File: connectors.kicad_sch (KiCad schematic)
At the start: 11 parts, among them J1 DE9_Pins_MountingHoles, J10 Conn_01x08_Socket, J11 Conn_01x08_Socket, J2 Conn_01x08_Socket, J3 HPF-02-01-X-S, J4 Conn_01x04_Socket, J5 Conn_01x04_Socket, J6 Conn_01x04_Socket, J7 Conn_01x04_Socket, J8 Conn_01x02_Pin, J9 Conn_01x02_Pin

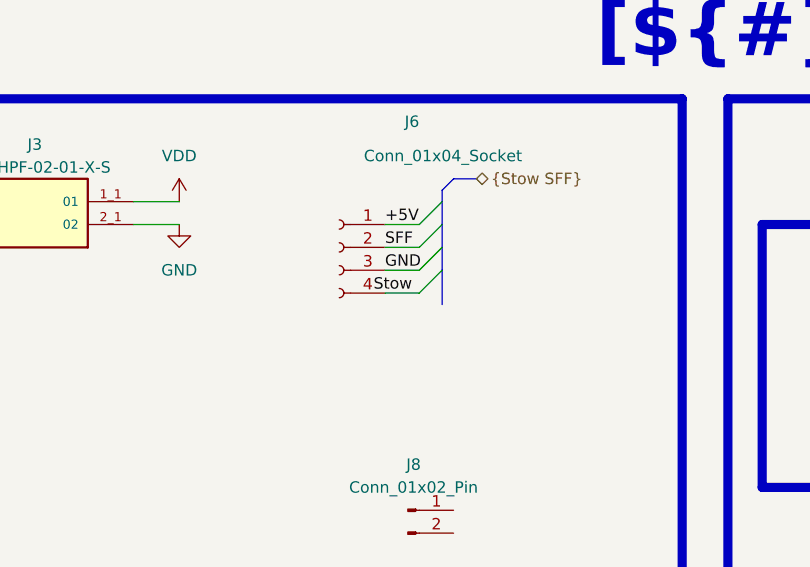
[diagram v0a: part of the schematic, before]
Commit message: updated architecture page
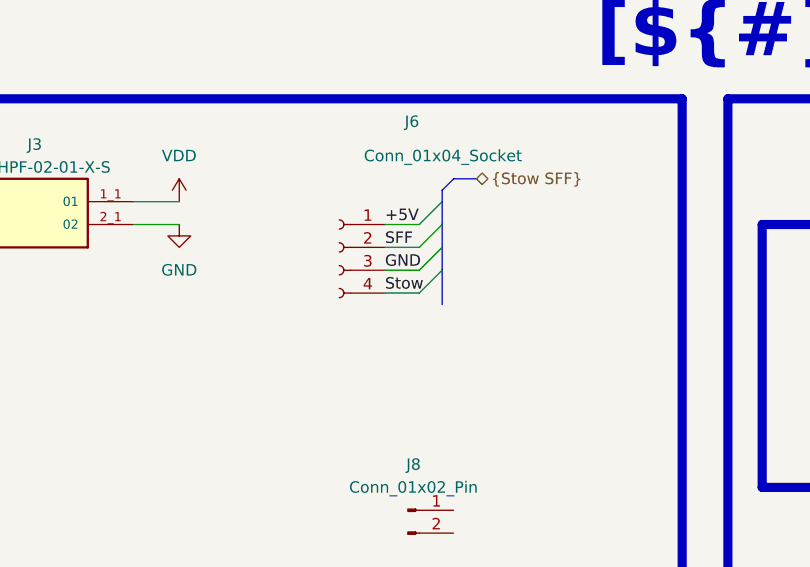
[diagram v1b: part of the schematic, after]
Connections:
- net Stow: now also J6.4 (Pin_4)
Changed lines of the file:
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@@
 	)
 	(label "Stow"
-		(at 107.95 48.26 0)
+		(at 109.22 48.26 0)
 		(effects
 			(font

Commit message: begin pcb
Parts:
- J1: footprint (none) -> Connector_Dsub:DSUB-9_Pins_Horizontal_P2.77x2.84mm_EdgePinOffset4.94mm_Housed_MountingHolesOffset4.94mm
- J10, J11: footprint (none) -> Connector_Molex:Molex_PicoBlade_53047-0810_1x08_P1.25mm_Vertical
- J2: footprint (none) -> Connector_PinHeader_2.54mm:PinHeader_1x08_P2.54mm_Vertical
- J3: footprint HPF-02-01-X-S:SAMTEC_HPF-02-01-X-S -> Connector_Samtec_HPM_THT:Samtec_HPM-02-05-x-S_Straight_1x02_Pitch5.08mm
- J4, J6: footprint (none) -> Connector_Molex:Molex_PicoBlade_53047-0410_1x04_P1.25mm_Vertical
- J5, J7: footprint (none) -> Connector_Molex:Molex_PicoBlade_53048-0410_1x04_P1.25mm_Horizontal
- J8: footprint (none) -> Connector_Molex:Molex_PicoBlade_53047-0210_1x02_P1.25mm_Vertical
- J9: footprint (none) -> Connector_Molex:Molex_PicoBlade_53048-0210_1x02_P1.25mm_Horizontal
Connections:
- net +5V: now also J8.1 (Pin_1), J8.2 (Pin_2), J9.1 (Pin_1), J9.2 (Pin_2)
- net +M: no longer J4.4 (Pin_4), J5.4 (Pin_4)
- net -M: no longer J4.3 (Pin_3), J5.3 (Pin_3)
- net RE1.A: now reaches J11.2 (Pin_2)
- net RE1.A: now also J10.2 (Pin_2)
- net RE1.B: now reaches J11.3 (Pin_3)
- net RE1.B: now also J10.3 (Pin_3)
- net RE1.C: now reaches J11.4 (Pin_4)
- net RE1.C: now also J10.4 (Pin_4)
- net RE2.A: now reaches J11.5 (Pin_5)
- net RE2.A: now also J10.5 (Pin_5)
- net RE2.B: now reaches J11.6 (Pin_6)
- net RE2.B: now also J10.6 (Pin_6)
- net RE2.C: now reaches J11.7 (Pin_7)
- net RE2.C: now also J10.7 (Pin_7)
- new net +MB: J4.4 (Pin_4), J5.4 (Pin_4)
- new net -MB: J4.3 (Pin_3), J5.3 (Pin_3)
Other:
- moved on the sheet: J9
